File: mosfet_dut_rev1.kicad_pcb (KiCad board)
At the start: 2 copper layers, 113.2 x 85 mm, 40 parts, among them J2 Conn, J3 Conn_01x02, J4 Conn_01x02, J5 Conn_01x02, J6 Conn_01x02, J7 USB_C_Receptacle_USB2.0_16P, Q1 AO3400A, Q2 AO3400A, Q3 AO3400A, Q4 AO3400A, U1 AP2112K-3.3, U2 USBLC6-2SC6, U4 INA219AxD, U6 ESP32-WROOM-32E, U7 CH340C

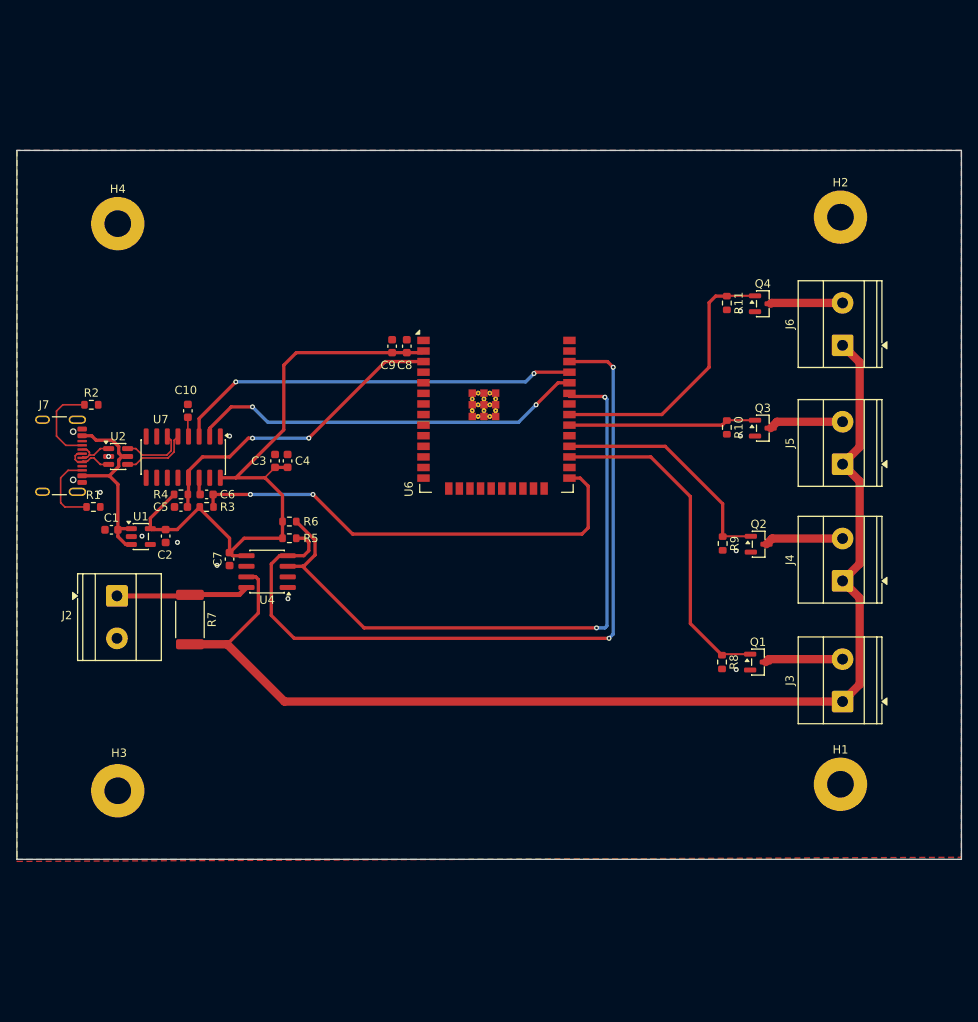
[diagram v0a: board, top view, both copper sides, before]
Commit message: Rev 1.1: Schematic Complete + BOM + JLCPCB Part Numbers
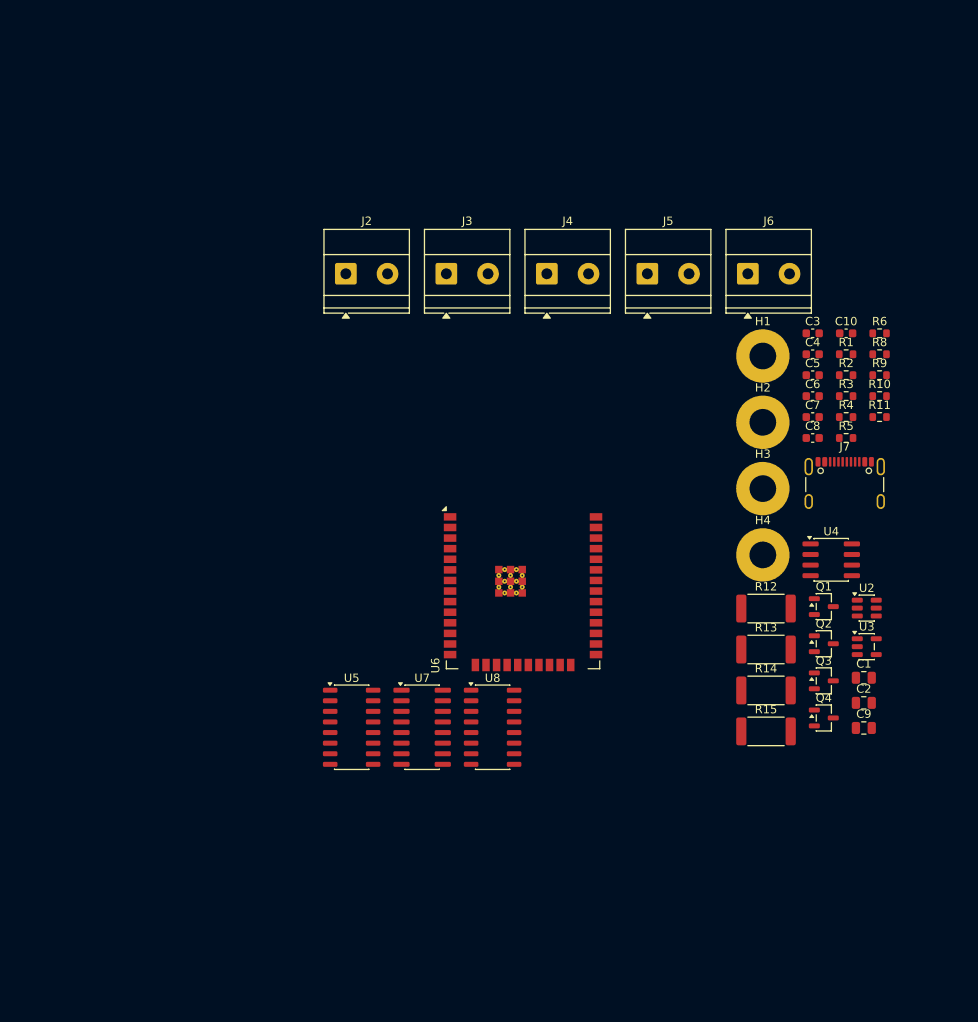
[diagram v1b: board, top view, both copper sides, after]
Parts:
- removed R7: 0.1, Resistor_SMD:R_2512_6332Metric
- removed U1: AP2112K-3.3, Package_TO_SOT_SMD:SOT-23-5
- added R12: 0.05, Resistor_SMD:R_2512_6332Metric, F.Cu at (179.8, 100.7)
- added R13: 0.05, Resistor_SMD:R_2512_6332Metric, F.Cu at (179.8, 105.6)
- added R14: 0.05, Resistor_SMD:R_2512_6332Metric, F.Cu at (179.8, 110.5)
- added R15: 0.05, Resistor_SMD:R_2512_6332Metric, F.Cu at (179.8, 115.4)
- added U3: ME6211C33M5, Package_TO_SOT_SMD:SOT-23-5, F.Cu at (191.9, 105.2)
- added U5: 74HC4051, Package_SO:SO-16_3.9x9.9mm_P1.27mm, F.Cu at (130.1, 114.9)
- added U8: 74HC4051, Package_SO:SO-16_3.9x9.9mm_P1.27mm, F.Cu at (147.0, 114.9)
- C1, C2, C9: footprint Capacitor_SMD:C_0603_1608Metric -> Capacitor_SMD:C_0805_2012Metric
- J2, J3, J4, J5, J6: footprint TerminalBlock_Phoenix:TerminalBlock_Phoenix_MKDS-1,5-2-5.08_1x02_P5.08mm_Horizontal -> TerminalBlock_Phoenix:TerminalBlock_Phoenix_MKDS-1,5-2_1x02_P5.00mm_Horizontal
- Q1, Q2, Q3, Q4: footprint Package_TO_SOT_SMD:SOT-23 -> Package_TO_SOT_SMD:SOT-23-3
- moved J7 95.2 mm to (189.3, 86.8), turned to 0 degrees
- moved R1 92.1 mm to (189.4, 70.2)
- moved C1 91.9 mm to (191.6, 109.0)
- moved U2 91.6 mm to (191.9, 100.6)
- moved R2 90.6 mm to (189.4, 72.7)
- moved H4 86.9 mm to (179.4, 94.2)
- moved C2 86.1 mm to (191.6, 112.0), turned to 0 degrees
- moved H3 85.4 mm to (179.4, 86.3)
- moved R4 80.3 mm to (189.4, 77.7)
- moved C10 79.5 mm to (189.4, 67.7), turned to 0 degrees
- moved R3 77.8 mm to (189.4, 75.2)
- moved C5 77.4 mm to (185.4, 72.7)
- moved R6 74.3 mm to (193.4, 67.7)
- moved C6 73.6 mm to (185.4, 75.2)
- moved C9 72.8 mm to (191.6, 115.0), turned to 0 degrees
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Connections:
- J3 pad 1: /POWER_BUS+ -> /OUT1+
- J4 pad 1: /POWER_BUS+ -> /OUT2+
- J5 pad 1: /POWER_BUS+ -> /OUT3+
- J6 pad 1: /POWER_BUS+ -> /OUT4+
- U4 pad 7: /POWER_BUS+ -> /IN-
- U4 pad 8: /POWER_SENSE+ -> /IN+
- U6 pad 10: unconnected-(U6-IO25-Pad10) -> /GPIO25
- U6 pad 11: unconnected-(U6-IO26-Pad11) -> /GPIO26
- U6 pad 12: unconnected-(U6-IO27-Pad12) -> /GPIO27
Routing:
- net /POWER_BUS+: track 139.8 -> 0.00 mm
- net /I2C_SCL: track 93.9 -> 0.00 mm, vias 2 -> 0
- net /I2C_SDA: track 80.3 -> 0.00 mm, vias 2 -> 0
- net +3V3: track 78.6 -> 0.00 mm
- net /BOOT: track 58.5 -> 0.00 mm, vias 2 -> 0
- net /ESP32 TX0: track 48.9 -> 0.00 mm, vias 2 -> 0
- net /ESP32 RX0: track 47.9 -> 0.00 mm, vias 2 -> 0
- net /M1_CTRL: track 40.5 -> 0.00 mm
- net /RESET: track 38.0 -> 0.00 mm, vias 2 -> 0
- net /M4_CTRL: track 32.7 -> 0.00 mm
- net /M2_CTRL: track 28.6 -> 0.00 mm
- net +VBUS: track 24.5 -> 0.00 mm
- net /M3_CTRL: track 22.5 -> 0.00 mm
- net /POWER_SENSE+: track 15.9 -> 0.00 mm
- net /USBD+: track 13.7 -> 0.00 mm
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- removed copper zone on B.Cu, net GND
- removed copper zone on F.Cu, net GND
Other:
- board outline removed

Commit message: Rev 1.1: Final Component Schematic + BOM
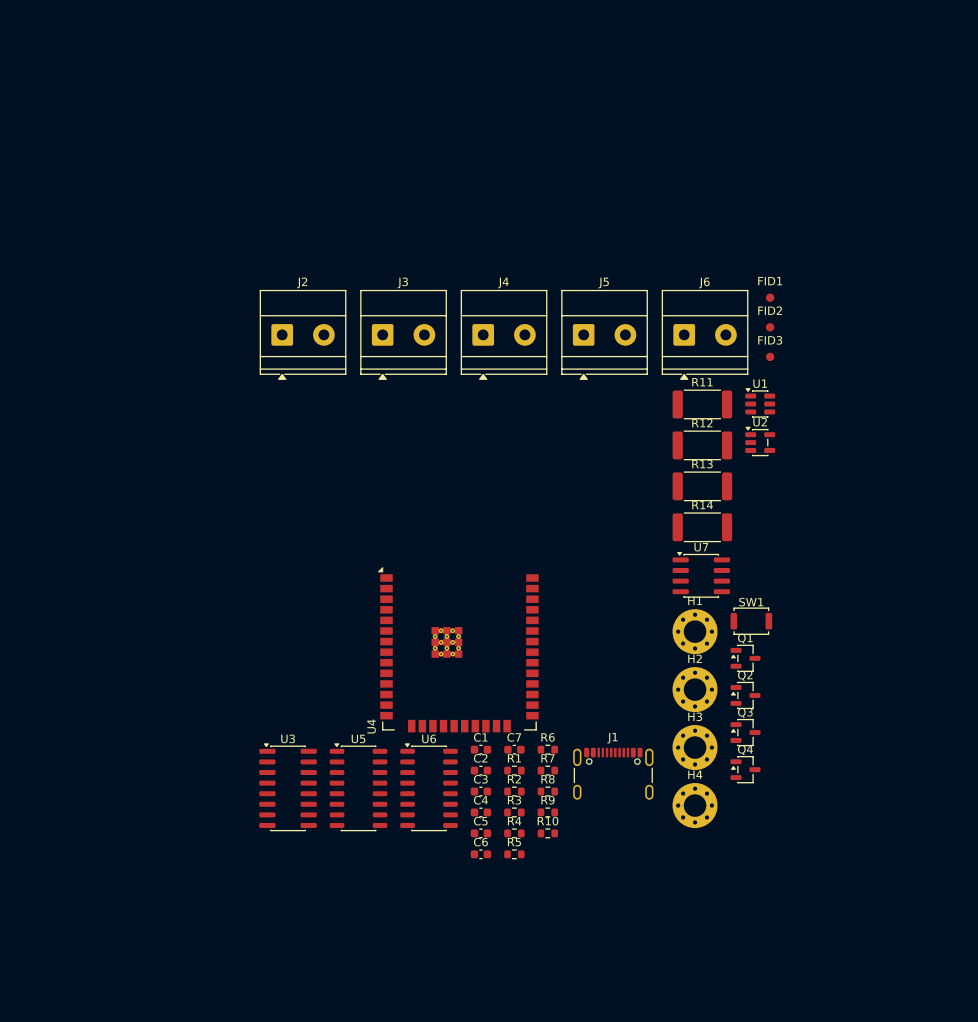
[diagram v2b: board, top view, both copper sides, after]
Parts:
- removed C10, C8: 0.1uF, Capacitor_SMD:C_0603_1608Metric
- removed C9: 1uF, Capacitor_SMD:C_0805_2012Metric
- removed J7: USB_C_Receptacle_USB2.0_16P, Connector_USB:USB_C_Receptacle_GCT_USB4105-xx-A_16P_TopMnt_Horizontal
- removed R15: 0.05, Resistor_SMD:R_2512_6332Metric
- removed U8: 74HC4051, Package_SO:SO-16_3.9x9.9mm_P1.27mm
- added FID1: Fiducial, Fiducial:Fiducial_1mm_Mask2mm, F.Cu at (180.3, 63.4)
- added FID2: Fiducial, Fiducial:Fiducial_1mm_Mask2mm, F.Cu at (180.3, 67.0)
- added FID3: Fiducial, Fiducial:Fiducial_1mm_Mask2mm, F.Cu at (180.3, 70.5)
- added J1: USB_C_Receptacle_USB2.0_16P, Connector_USB:USB_C_Receptacle_GCT_USB4105-xx-A_16P_TopMnt_Horizontal, F.Cu at (161.5, 121.6)
- added R7: 5k1, Resistor_SMD:R_0603_1608Metric, F.Cu at (153.7, 120.1)
- added SW1: SW_Push, Button_Switch_SMD:SW_Push_SPST_NO_Alps_SKRK, F.Cu at (178.1, 102.2)
- added U1: USBLC6-2SC6, Package_TO_SOT_SMD:SOT-23-6, F.Cu at (179.1, 76.2)
- C1, C2: value 1u -> 1uF; footprint Capacitor_SMD:C_0805_2012Metric -> Capacitor_SMD:C_0603_1608Metric
- C3, C4: value 470n -> 0.1uF
- C6: value 0.1uF -> 10uF
- H1, H2, H3, H4: value MountingHole -> MountingHole_Pad; footprint MountingHole:MountingHole_3.2mm_M3_Pad -> MountingHole:MountingHole_2.7mm_Pad_Via
- J2: value Conn -> Conn_01x02
- R11: value 5k1 -> 50m; footprint Resistor_SMD:R_0603_1608Metric -> Resistor_SMD:R_2512_6332Metric
- R12, R13, R14: value 0.05 -> 50m
- U2: value USBLC6-2SC6 -> ME6211C33M5; footprint Package_TO_SOT_SMD:SOT-23-6 -> Package_TO_SOT_SMD:SOT-23-5
- U3: value ME6211C33M5 -> CH340C; footprint Package_TO_SOT_SMD:SOT-23-5 -> Package_SO:SOIC-16_3.9x9.9mm_P1.27mm
- U4: value INA219AxD -> ESP32-WROOM-32E; footprint Package_SO:SOIC-8_3.9x4.9mm_P1.27mm -> RF_Module:ESP32-WROOM-32E
- U6: value ESP32-WROOM-32E -> 74HC4051; footprint RF_Module:ESP32-WROOM-32E -> Package_SO:SO-16_3.9x9.9mm_P1.27mm
- U7: value CH340C -> INA219AxD; footprint Package_SO:SOIC-16_3.9x9.9mm_P1.27mm -> Package_SO:SOIC-8_3.9x4.9mm_P1.27mm
- moved U3 71.4 mm to (122.5, 122.2)
- moved C6 67.8 mm to (145.6, 130.2)
- moved C3 67.8 mm to (145.6, 122.6)
- moved C4 67.8 mm to (145.6, 125.1)
- moved C5 67.8 mm to (145.6, 127.6)
- moved R10 65.8 mm to (153.7, 127.6)
- moved R8 65.8 mm to (153.7, 122.6)
- moved R9 65.8 mm to (153.7, 125.1)
- moved R1 63.8 mm to (149.7, 120.1)
- moved R2 63.8 mm to (149.7, 122.6)
- moved R3 63.8 mm to (149.7, 125.1)
- moved R4 63.8 mm to (149.7, 127.6)
- moved R5 63.8 mm to (149.7, 130.2)
- moved R6 63.8 mm to (153.7, 117.6)
- moved C7 53.6 mm to (149.7, 117.6)
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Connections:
- C3 pad 1: +3V3 -> /UARTDDTR
- C3 pad 2: GND -> /UARTDDTR
- C4 pad 1: +3V3 -> /UARTDRTS
- C4 pad 2: GND -> /UARTDRTS
- C5 pad 1: /RESET -> GND
- C5 pad 2: /RESET -> +3V3
- C6 pad 1: /BOOT -> GND
- C6 pad 2: /BOOT -> +3V3
- H1 pad 1: (no net) -> GND
- H2 pad 1: (no net) -> GND
- H3 pad 1: (no net) -> GND
- H4 pad 1: (no net) -> GND
- R10 pad 1: /M3_CTRL -> +3V3
- R10 pad 2: GND -> /I2C_SCL
- R11 pad 1: /M4_CTRL -> /OUT1+
- R11 pad 2: GND -> /POWER_SENSE+
- R12 pad 1: /OUT1+ -> /OUT2+
- R13 pad 1: /OUT2+ -> /OUT3+
- R14 pad 1: /OUT3+ -> /OUT4+
- R3 pad 2: /BOOT -> /UARTDDTR
- R4 pad 2: /RESET -> /UARTDRTS
- R5 pad 1: +3V3 -> /M1_CTRL
- R5 pad 2: /I2C_SCL -> GND
- R6 pad 1: +3V3 -> /M2_CTRL
- R6 pad 2: /I2C_SDA -> GND
- R8 pad 1: /M1_CTRL -> /M4_CTRL
- R9 pad 1: /M2_CTRL -> +3V3
- R9 pad 2: GND -> /I2C_SDA
- U2 pad 1: /USBD- -> +VBUS
- U2 pad 3: /USBD+ -> +VBUS
- U2 pad 4: /USBD- -> unconnected-(U2-NC-Pad4)
- U2 pad 5: +VBUS -> +3V3
- U3 pad 1: +VBUS -> GND
- U3 pad 2: GND -> /UARTDRX
- U3 pad 3: +VBUS -> /UARTDTX
- U3 pad 4: unconnected-(U3-NC-Pad4) -> +3V3
- U3 pad 5: +3V3 -> /USBD+
- U4 pad 2: GND -> +3V3
- U4 pad 3: /I2C_SDA -> /UARTDDTR
- U4 pad 4: /I2C_SCL -> unconnected-(U4-SENSOR_VP-Pad4)
- U4 pad 5: +3V3 -> unconnected-(U4-SENSOR_VN-Pad5)
- U4 pad 6: GND -> /I2C_SDA
- U4 pad 7: /IN- -> /I2C_SCL
- U4 pad 8: /IN+ -> unconnected-(U4-IO32-Pad8)
- U6 pad 1: GND -> unconnected-(U6-A4-Pad1)
- U6 pad 10: /GPIO25 -> /GPIO26
- U6 pad 11: /GPIO26 -> /GPIO25
- U6 pad 12: /GPIO27 -> /OUT1+
- U6 pad 13: unconnected-(U6-IO14-Pad13) -> /OUT2+
- U6 pad 14: unconnected-(U6-IO12-Pad14) -> /OUT3+
- U6 pad 15: GND -> /OUT4+
- U6 pad 16: unconnected-(U6-IO13-Pad16) -> +3V3
- U6 pad 2: +3V3 -> unconnected-(U6-A6-Pad2)
- U6 pad 3: /RESET -> /IN-
- U6 pad 6: unconnected-(U6-IO34-Pad6) -> GND
- U6 pad 7: unconnected-(U6-IO35-Pad7) -> GND
- U6 pad 8: unconnected-(U6-IO32-Pad8) -> GND
- U6 pad 9: unconnected-(U6-IO33-Pad9) -> /GPIO27
- U7 pad 2: /ESP32 RX0 -> GND
- U7 pad 3: /ESP32 TX0 -> /I2C_SDA
- U7 pad 4: Net-(U7-V3) -> /I2C_SCL
- U7 pad 5: /USBD- -> +3V3
- U7 pad 6: /USBD+ -> GND
- U7 pad 7: unconnected-(U7-NC-Pad7) -> /IN-
- U7 pad 8: unconnected-(U7-NC-Pad8) -> /IN+
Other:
- rule pad_to_mask_clearance: 0 -> 0.1

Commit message: Rev 1.1: Board placement and rough tracks
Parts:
- removed the U5 at (131.0, 122.2)
- moved H1 95.3 mm to (105.3, 34.7)
- moved J1 81.1 mm to (106.2, 62.3), turned to -90 degrees
- moved C6 78.7 mm to (136.7, 51.9), turned to -90 degrees
- moved R4 78.4 mm to (123.5, 53.8), turned to -90 degrees
- moved H2 77.7 mm to (187.5, 34.4)
- moved R2 77.0 mm to (111.0, 56.1)
- moved R3 76.5 mm to (122.0, 53.8), turned to -90 degrees
- moved C5 76.1 mm to (138.2, 51.9), turned to -90 degrees
- moved R5 76.0 mm to (161.8, 55.1), turned to -90 degrees
- moved C2 73.5 mm to (118.9, 51.7), turned to 90 degrees
- moved H4 73.2 mm to (105.4, 92.4)
- moved C1 72.7 mm to (114.9, 51.7), turned to -90 degrees
- moved C4 71.9 mm to (123.5, 56.8), turned to -90 degrees
- moved R10 71.3 mm to (136.2, 58.5), turned to -90 degrees
- moved C3 70.0 mm to (122.0, 56.8), turned to 90 degrees
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- renumbered U6 to U5, U7 to U6
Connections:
- J1 pad A6: /USBD+ -> /USBCD+
- J1 pad A7: /USBD- -> /USBCD-
- J1 pad B6: /USBD+ -> /USBCD+
- J1 pad B7: /USBD- -> /USBCD-
- U1 pad 1: /USBD- -> /USBCD-
- U1 pad 3: /USBD+ -> /USBCD+
- U4 pad 27: /M1_CTRL -> /M4_CTRL
- U4 pad 28: /M2_CTRL -> /M3_CTRL
- U4 pad 30: /M3_CTRL -> /M2_CTRL
- U4 pad 31: /M4_CTRL -> /M1_CTRL
- U4 pad 6: /I2C_SDA -> /I2C_SCL
- U4 pad 7: /I2C_SCL -> /I2C_SDA
- U5 pad 1: unconnected-(U6-A4-Pad1) -> /OUT4+
- U5 pad 12: /OUT1+ -> unconnected-(U5-A3-Pad12)
- U5 pad 13: /OUT2+ -> unconnected-(U5-A0-Pad13)
- U5 pad 14: /OUT3+ -> unconnected-(U5-A1-Pad14)
- U5 pad 15: /OUT4+ -> unconnected-(U5-A2-Pad15)
- U5 pad 2: unconnected-(U6-A6-Pad2) -> /OUT3+
- U5 pad 4: unconnected-(U6-A7-Pad4) -> /OUT2+
- U5 pad 5: unconnected-(U6-A5-Pad5) -> /OUT1+
- U6 pad 8: /IN+ -> /POWER_SENSE+
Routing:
- net /OUT4+: track 0.00 -> 80.1 mm
- net /OUT3+: track 0.00 -> 68.8 mm
- net /OUT2+: track 0.00 -> 61.2 mm
- net /OUT1+: track 0.00 -> 58.9 mm
- net /POWER_SENSE+: track 0.00 -> 58.5 mm

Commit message: Rev 1.1: Final
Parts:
- moved FID3 90.4 mm to (178.0, 114.0)
- moved FID2 73.2 mm to (111.0, 114.0)
- moved R3 29.7 mm to (112.8, 82.0), turned to 0 degrees
- moved FID1 28.7 mm to (111.0, 65.1)
- moved R1 26.0 mm to (103.5, 93.5)
- moved J3 25.7 mm to (180.0, 108.5)
- moved J4 25.7 mm to (180.0, 96.4)
- moved U5 25.7 mm to (127.5, 105.2)
- moved C7 25.7 mm to (114.9, 93.0)
- moved Q3 25.7 mm to (158.8, 88.7)
- moved R7 25.7 mm to (154.4, 88.7)
- moved U6 25.7 mm to (118.7, 96.2)
- moved C6 25.7 mm to (129.3, 76.5)
- moved J1 25.7 mm to (98.8, 86.9)
- moved J5 25.7 mm to (180.0, 84.3)
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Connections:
- C3 pad 2: /UARTDDTR -> /UARTDDTR_EN
- C4 pad 1: /UARTDRTS -> /UARTDRTS_IO0
- R3 pad 2: /UARTDDTR -> /UARTDRTS_IO0
- R4 pad 2: /UARTDRTS -> /UARTDDTR_EN
- SW1 pad 2: /UARTDDTR -> /UARTDDTR_EN
- U4 pad 25: /UARTDRTS -> /UARTDRTS_IO0
- U4 pad 3: /UARTDDTR -> /UARTDDTR_EN
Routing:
- net /OUT1-: track 0.00 -> 82.3 mm
- net +3V3: track 0.00 -> 78.2 mm, vias 0 -> 2
- net /OUT2-: track 0.00 -> 69.2 mm
- net /OUT3-: track 0.00 -> 56.6 mm
- net /UARTDRX: track 0.00 -> 45.2 mm, vias 0 -> 6
- net /UARTDTX: track 0.00 -> 44.5 mm, vias 0 -> 6
- net /UARTDRTS_IO0: track 0.00 -> 43.7 mm, vias 0 -> 2
- net /OUT4-: track 0.00 -> 40.8 mm
- net +VBUS: track 0.00 -> 26.8 mm, vias 0 -> 2
- net /IN-: track 0.00 -> 21.7 mm
- net /I2C_SCL: track 0.00 -> 20.6 mm
- net /I2C_SDA: track 0.00 -> 20.5 mm
- net /UARTDDTR_EN: track 0.00 -> 19.3 mm, vias 0 -> 2
- net /GPIO25: track 0.00 -> 18.0 mm
- net /GPIO26: track 0.00 -> 16.2 mm
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- added copper zone on B.Cu, net GND
- added copper zone on F.Cu, net GND
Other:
- board outline added: 96.5 x 64.2 mm
- board text added: "+"
- board text added: "DC INPUT 3-24 VDC 2A MAX"
- board text added: "DUT Test Board Rev1.1"
